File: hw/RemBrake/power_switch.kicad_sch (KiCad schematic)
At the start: 54 parts, among them Q1 SiS415DNT, Q2 BC337, Q3 BC847, Q4 BC337, Q5 BC847, Q6 BC337, Q7 BC847, U1 TPS62140, U2 BD5230G-TR, U3 XC6220B331MR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

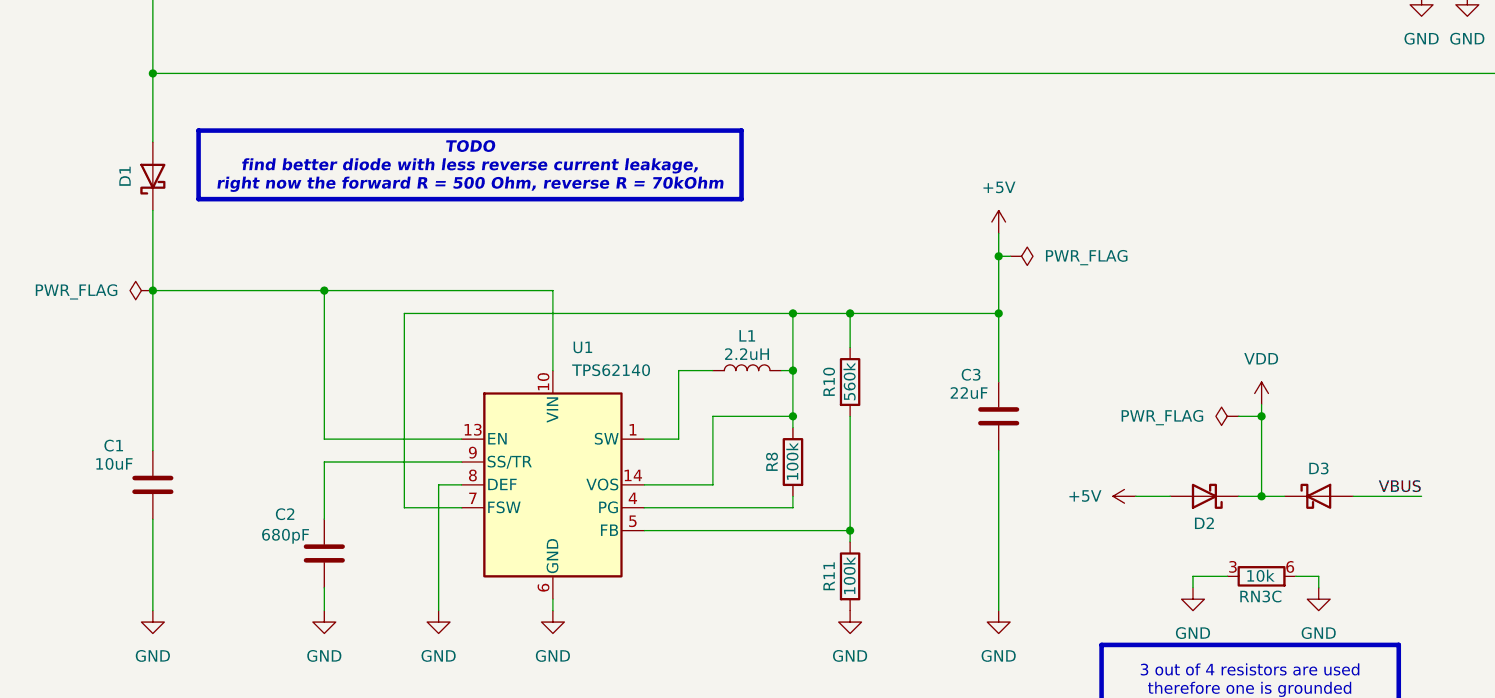
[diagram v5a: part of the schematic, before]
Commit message: added protection diode at the power input
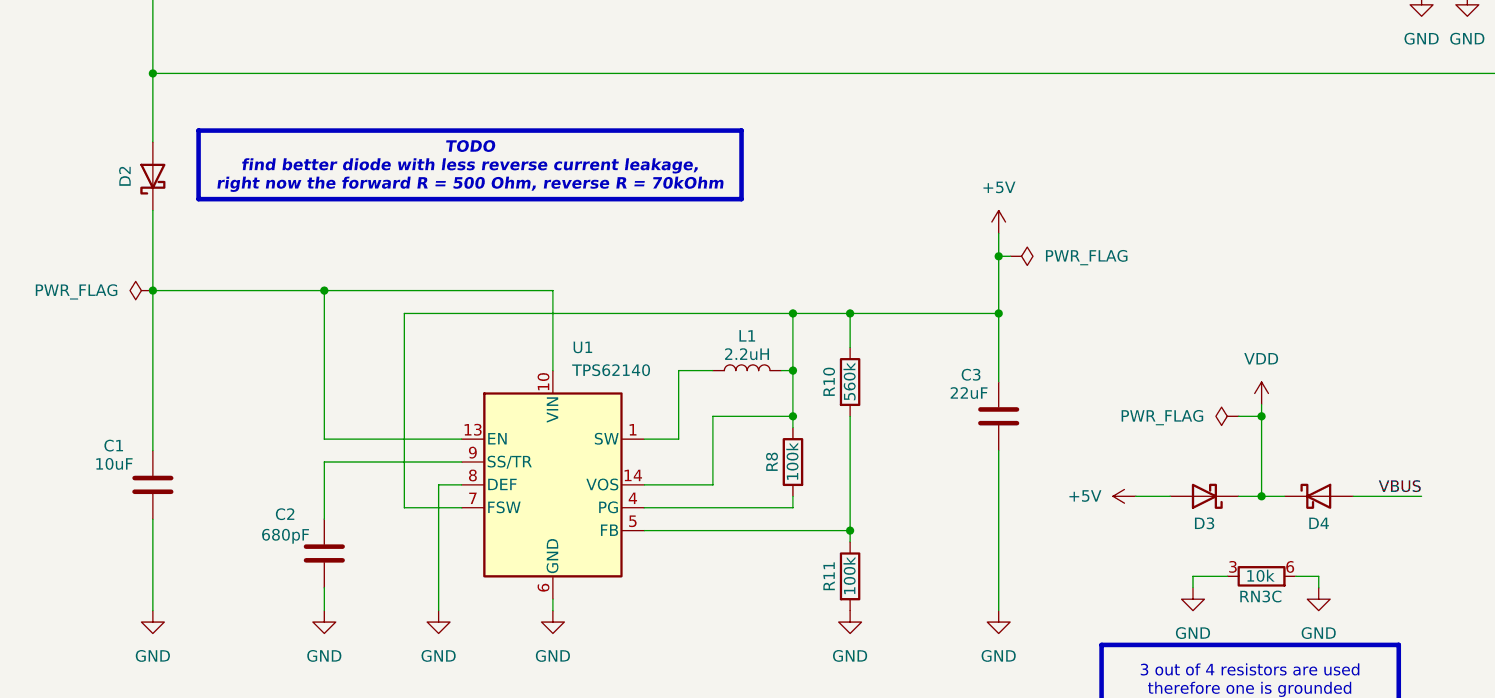
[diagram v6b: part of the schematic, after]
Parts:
- renumbered D1 to D2, D2 to D3, D3 to D4
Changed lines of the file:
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@@
 (kicad_sch
-	(version 20250513)
+	(version 20250610)
 	(generator "eeschema")
 	(generator_version "9.99")
@@
 		(on_board yes)
 		(dnp no)
-		(property "Reference" "D1"
+		(property "Reference" "D2"
 			(at 26.162 135.89 0)
 			(effects
@@
 			(project "RemBrake"
 				(path "/e6d4ae5b-c9d7-4cbe-b288-c929fdf55a75/2d0cc746-3115-4ebf-adba-86e7fd6ac8bd"
-					(reference "D1")
+					(reference "D2")
 					(unit 1)
 				)
@@
 		(on_board yes)
 		(dnp no)
-		(property "Reference" "D2"
+		(property "Reference" "D3"
 			(at 146.05 174.498 0)
 			(effects
@@
 			(project "RemBrake"
 				(path "/e6d4ae5b-c9d7-4cbe-b288-c929fdf55a75/2d0cc746-3115-4ebf-adba-86e7fd6ac8bd"
-					(reference "D2")
+					(reference "D3")
 					(unit 1)
 				)
@@
 		(on_board yes)
 		(dnp no)
-		(property "Reference" "D3"
-			(at 158.75 168.402 0)
+		(property "Reference" "D4"
+			(at 158.75 174.498 0)
 			(effects
 				(font
@@
 			(project "RemBrake"
 				(path "/e6d4ae5b-c9d7-4cbe-b288-c929fdf55a75/2d0cc746-3115-4ebf-adba-86e7fd6ac8bd"
-					(reference "D3")
+					(reference "D4")
 					(unit 1)
 				)

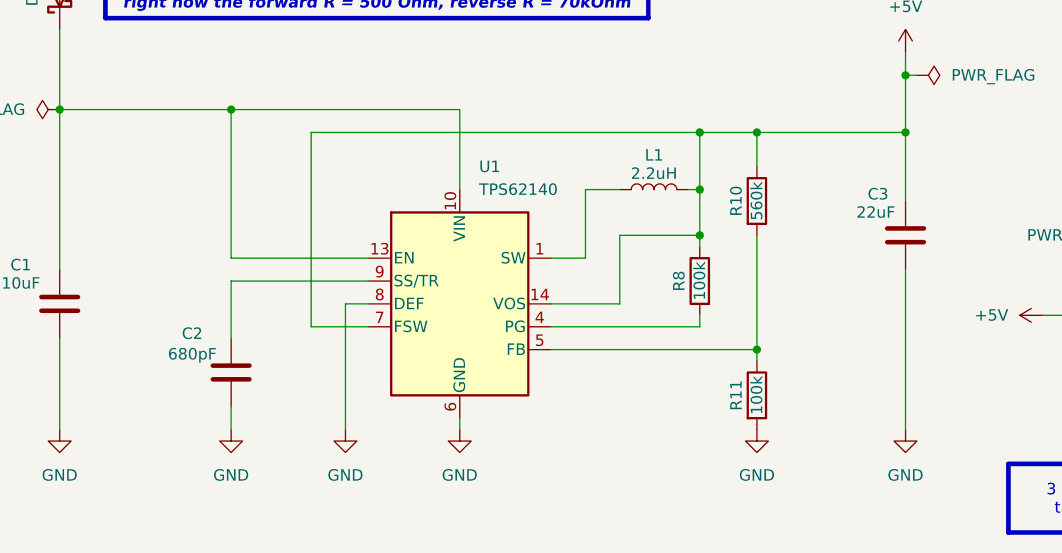
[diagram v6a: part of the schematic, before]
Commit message: updated BOM list and reduced number of different capacitors and resistors
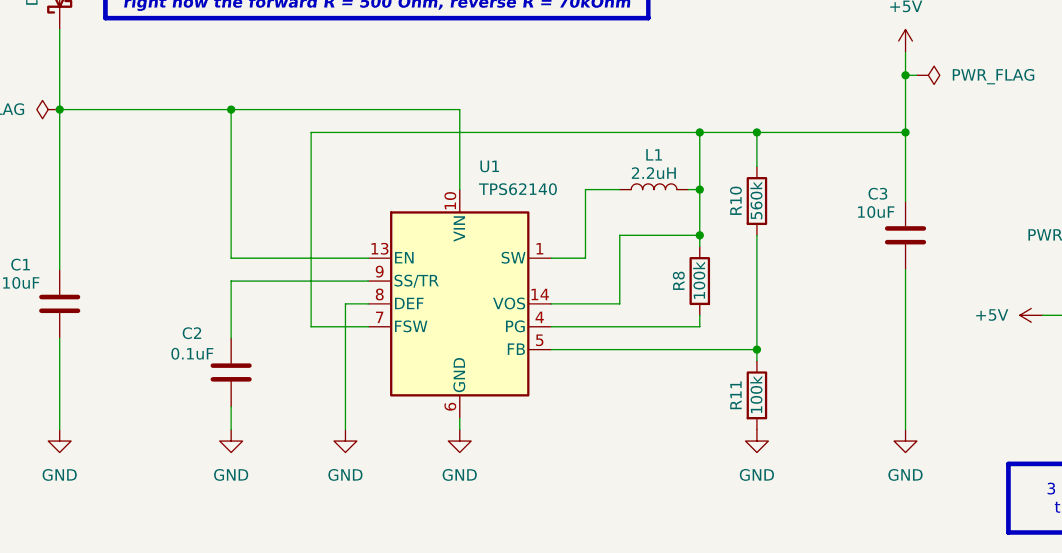
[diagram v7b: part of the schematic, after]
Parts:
- C2: value 680pF -> 0.1uF
- C3: value 22uF -> 10uF
- D2: value MBR0520 -> SS1200
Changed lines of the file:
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@@
 			)
 		)
-		(property "Value" "MBR0520"
+		(property "Value" "SS1200"
 			(at 25.4 136.2075 0)
 			(hide yes)
@@
 			)
 		)
-		(property "Value" "22uF"
+		(property "Value" "10uF"
 			(at 119.888 160.02 0)
 			(effects
@@
 			)
 		)
-		(property "Value" "680pF"
+		(property "Value" "0.1uF"
 			(at 43.942 175.768 0)
 			(effects
